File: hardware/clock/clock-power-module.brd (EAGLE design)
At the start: 29.2 x 39 mm, 13 parts, among them U3 L7805, U5 LTC6900IS5PBF

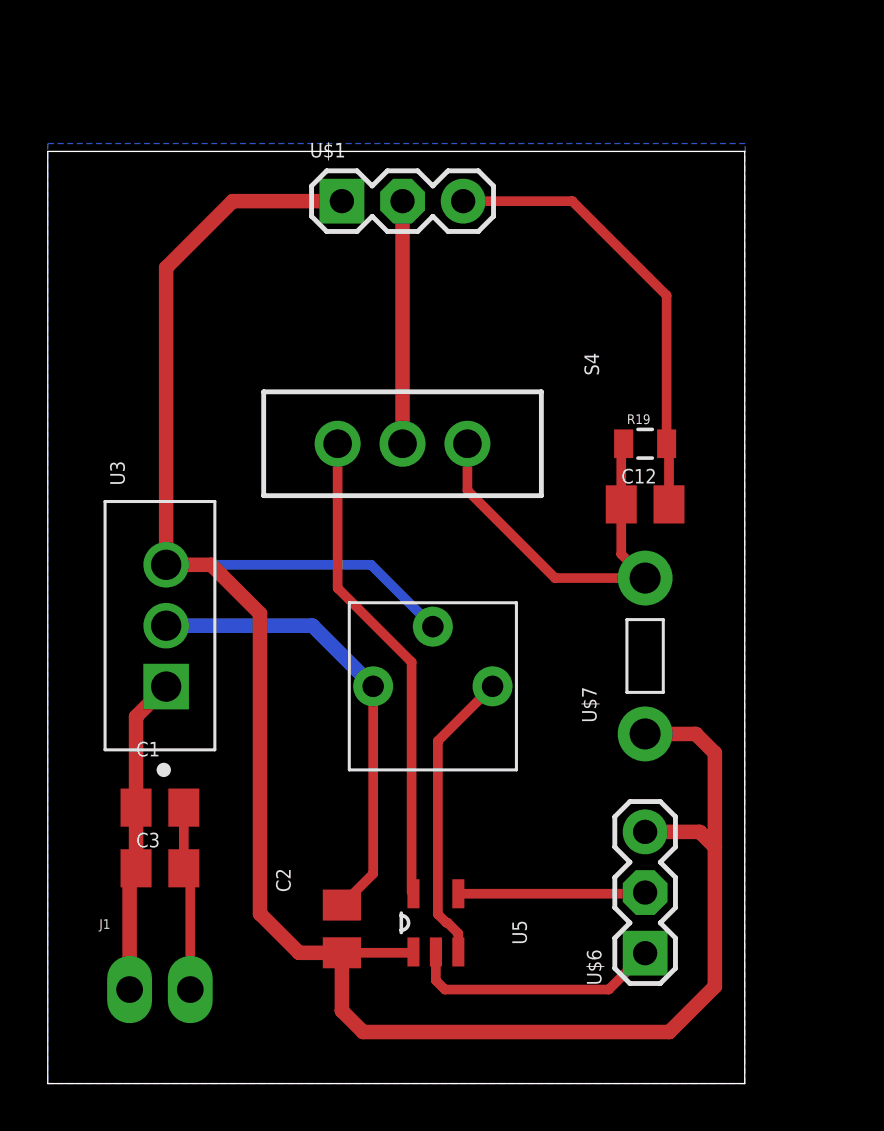
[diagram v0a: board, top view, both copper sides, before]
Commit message: update on clock board, so much cleaner now re-layout of main board
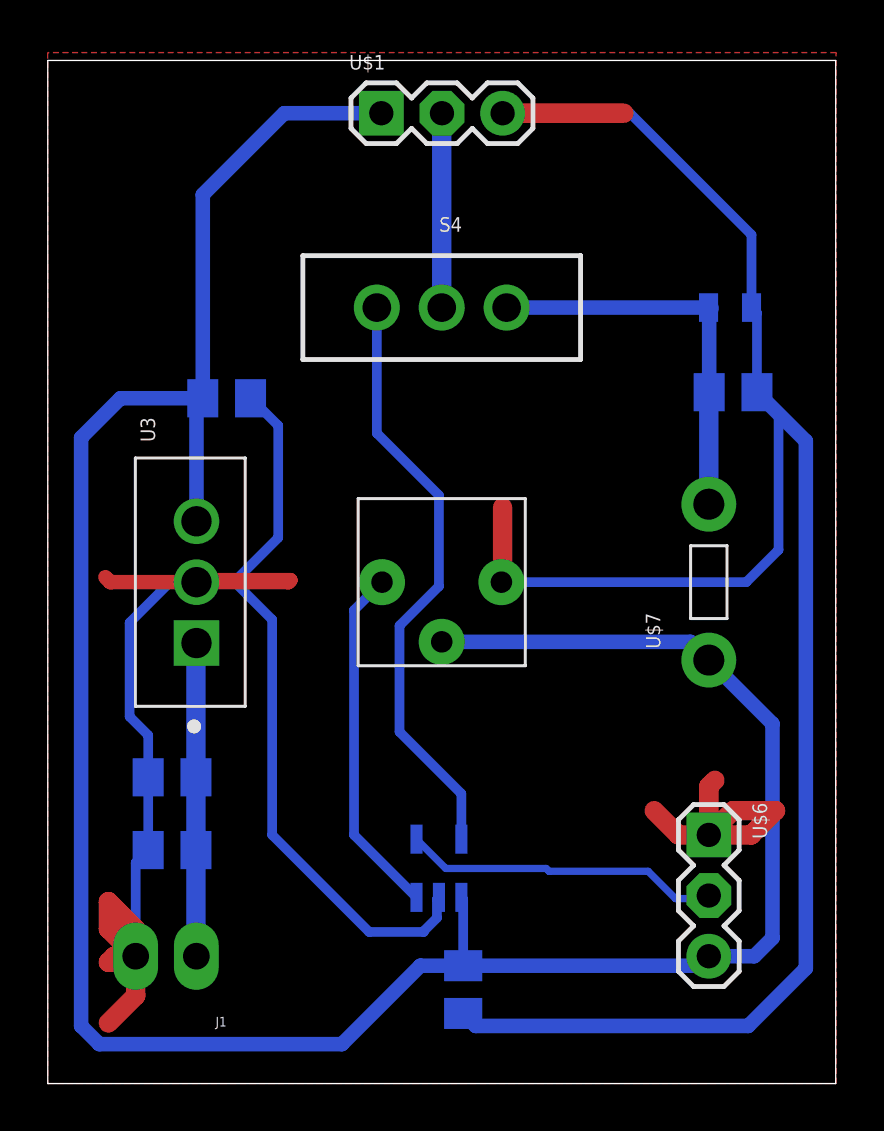
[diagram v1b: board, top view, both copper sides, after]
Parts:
- added C4: 0.1 uF, passives:C0805K
- moved C2 22.7 mm to (7.49, 28.7), flipped to the bottom, turned to 180 degrees
- moved R19 6.72 mm to (28.6, 32.5), flipped to the bottom, turned to 180 degrees
- moved C12 5.97 mm to (28.7, 29.0), flipped to the bottom, turned to 180 degrees
- moved S4 5.93 mm to (16.5, 32.5)
- moved U$6 5.63 mm to (27.7, 10.4), turned to 270 degrees
- moved U$3 4.38 mm to (16.5, 21.0), turned to 180 degrees
- moved U$7 4.08 mm to (27.7, 21.0)
- moved U$1 4.04 mm to (14.0, 40.6)
- moved J1 3.12 mm to (6.22, 5.33), turned to 180 degrees
- moved U5 2.29 mm to (16.4, 9.02), flipped to the bottom
- moved U3 2.22 mm to (5.97, 21.0)
- moved C1 1.37 mm to (5.21, 12.8), flipped to the bottom
- moved C3 0.92 mm to (5.21, 9.78), flipped to the bottom
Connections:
- net GND: now also C4.2
- net V5: now also C4.1
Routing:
- net GND: track 56.9 -> 172.9 mm
- net V5: track 93.1 -> 111.3 mm
- net DIV: track 7.84 -> 13.3 mm
- net VARIABLE_CLK_OUT: track 20.2 -> 25.1 mm
- net N$22: track 12.5 -> 14.8 mm
- net SYS_CLK: track 10.2 -> 8.14 mm
- added copper zone on layer 1, net GND
- removed copper zone on layer 16, net GND
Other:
- board size 29.2 x 39 mm -> 33 x 42.9 mm
